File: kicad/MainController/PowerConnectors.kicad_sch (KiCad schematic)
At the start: 26 parts, among them J4 H-Bridge, J5 Lamp, J7 RGB, J8 Winch, J9 Motor, Q1 BC547, Q10 BUZ11, Q2 BUZ11, Q3 BC547, Q4 BUZ11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

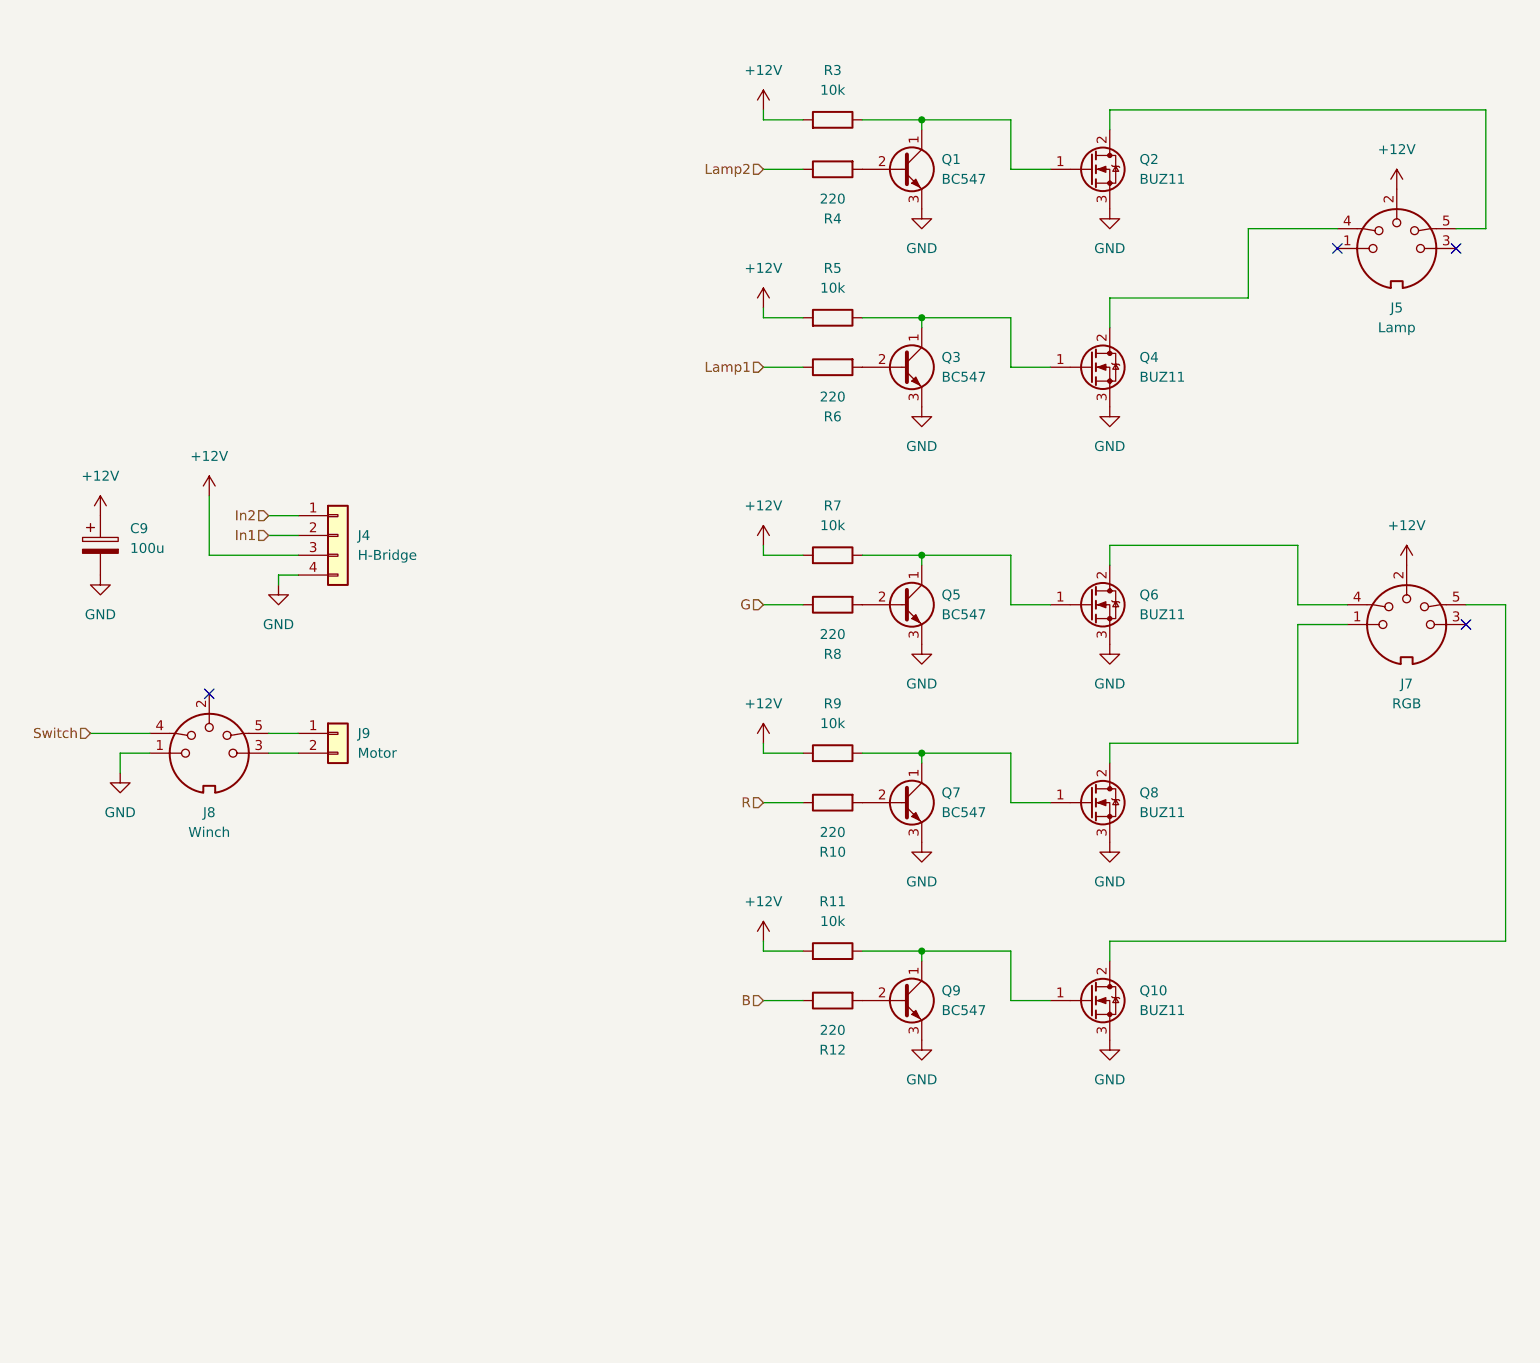
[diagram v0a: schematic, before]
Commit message: New main controller PCB layout using ESP32
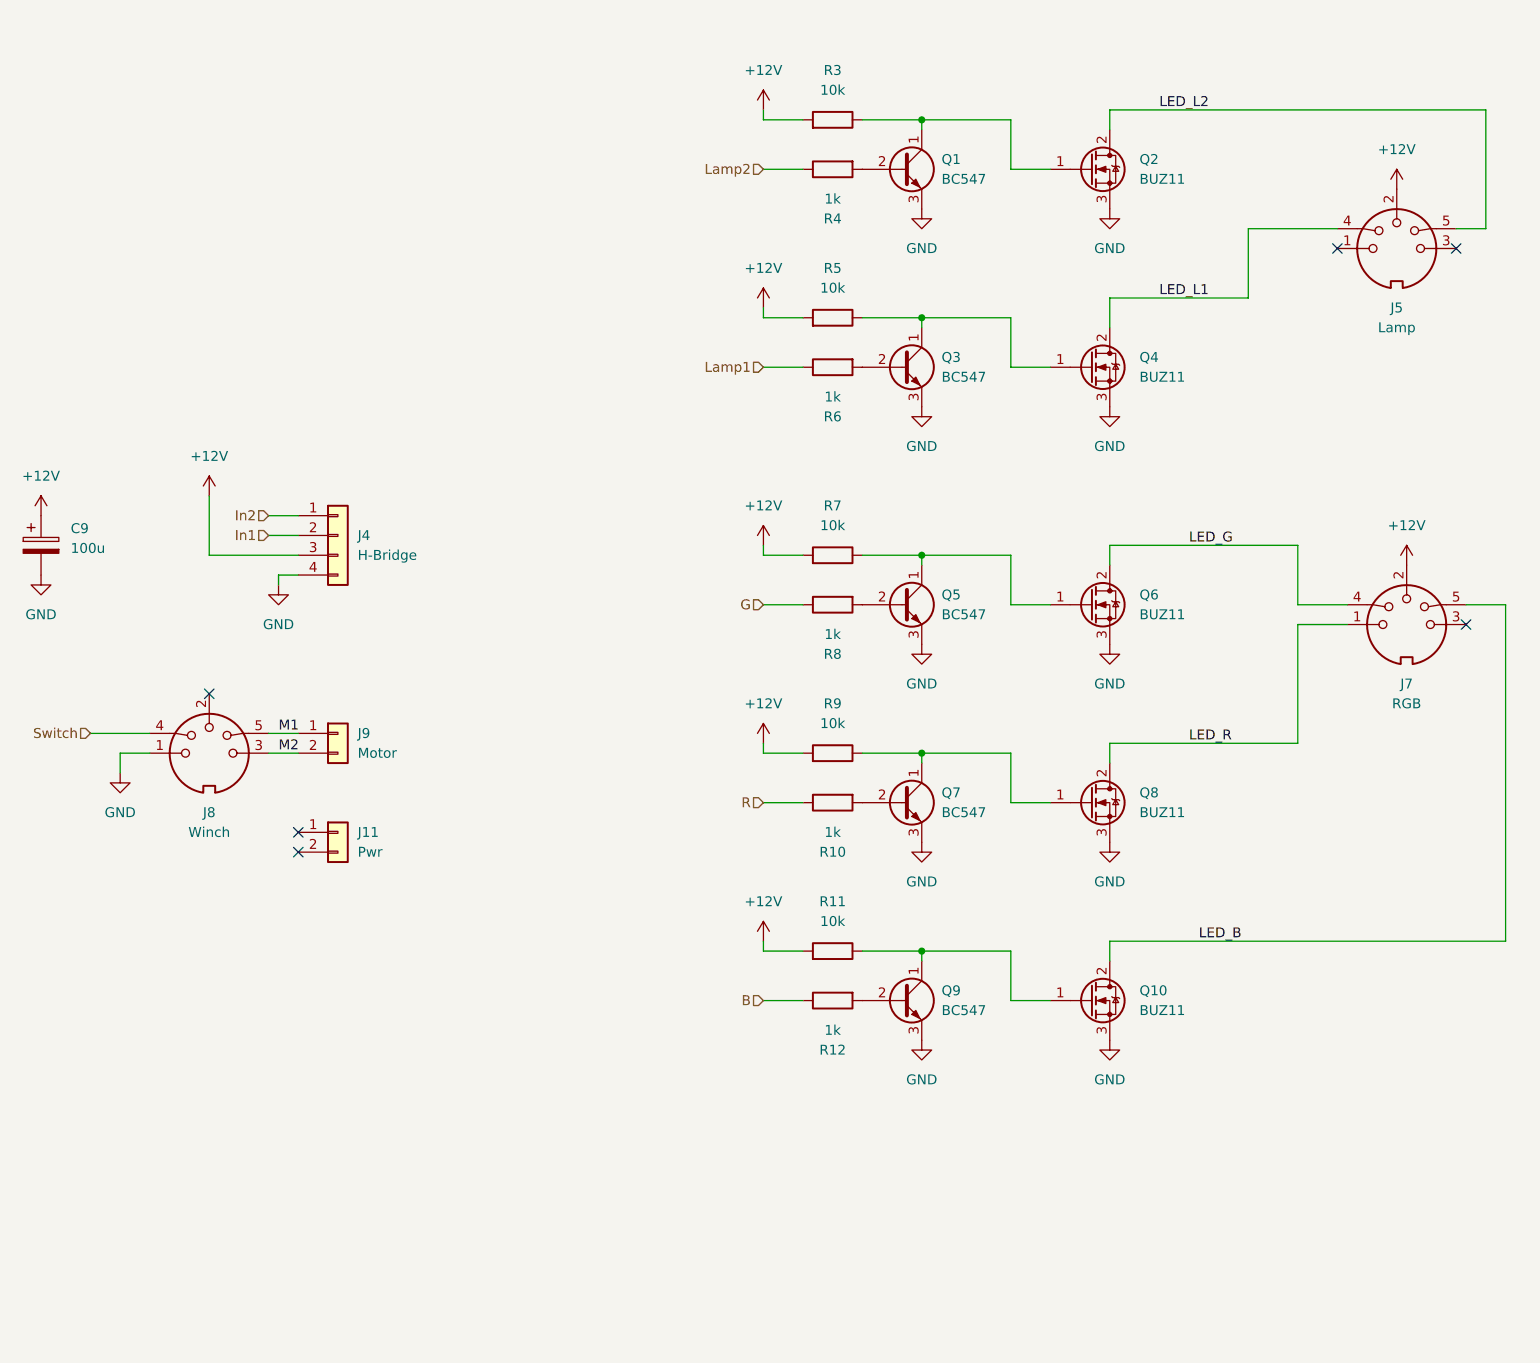
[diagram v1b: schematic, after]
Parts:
- added J11: Pwr, Connector_PinHeader_2.54mm:PinHeader_1x02_P2.54mm_Vertical, symbol Connector_Generic:Conn_01x02
- Q1, Q3, Q5, Q7, Q9: footprint Package_TO_SOT_THT:TO-92_Inline -> Custom_Footprints:TO-92_Milling
- R10, R12, R4, R6, R8: value 220 -> 1k; footprint Resistor_THT:R_Axial_DIN0204_L3.6mm_D1.6mm_P2.54mm_Vertical -> Resistor_THT:R_Axial_DIN0207_L6.3mm_D2.5mm_P10.16mm_Horizontal
- R11, R3, R5, R7, R9: footprint Resistor_THT:R_Axial_DIN0204_L3.6mm_D1.6mm_P2.54mm_Vertical -> Resistor_THT:R_Axial_DIN0207_L6.3mm_D2.5mm_P2.54mm_Vertical
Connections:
- net LED_L2: now reaches J5.5, Q2.2 (D)
- net LED_R: now reaches J7.1, Q8.2 (D)
- net LED_G: now reaches J7.4, Q6.2 (D)
- net LED_B: now reaches J7.5, Q10.2 (D)
- net LED_L1: now reaches J5.4, Q4.2 (D)
- net M1: now reaches J8.5, J9.1 (Pin_1)
- net M2: now reaches J8.3, J9.2 (Pin_2)
- no-connect marks 4 -> 6
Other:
- moved on the sheet: C9
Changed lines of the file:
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@@
 	)
 	(no_connect
+		(at 83.82 127)
+	)
+	(no_connect
 		(at 233.68 97.79)
 	)
@@
 	)
 	(no_connect
-		(at 232.41 49.53)
+		(at 83.82 124.46)
 	)
-	(wire
-		(pts
-			(xy 80.01 111.76) (xy 83.82 111.76)
-		)
-		(stroke
-			(width 0)
-			(type default)
-		)
+	(no_connect
+		(at 232.41 49.53)
 	)
 	(wire
@@
 	(wire
 		(pts
+			(xy 80.01 111.76) (xy 83.82 111.76)
+		)
+		(stroke
+			(width 0)
+			(type default)
+		)
+	)
+	(wire
+		(pts
 			(xy 156.21 139.7) (xy 163.83 139.7)
 		)
@@
 		)
 	)
+	(label "M2"
+		(at 81.28 114.3 0)
+		(effects
+			(font
+				(size 1.27 1.27)
+			)
+			(justify left bottom)
+		)
+	)
+	(label "M1"
+		(at 81.28 111.76 0)
+		(effects
+			(font
+				(size 1.27 1.27)
+			)
+			(justify left bottom)
+		)
+	)
+	(label "LED_B"
+		(at 199.39 138.43 0)
+		(effects
+			(font
+				(size 1.27 1.27)
+			)
+			(justify left bottom)
+		)
+	)
+	(label "LED_L1"
+		(at 194.31 55.88 0)
+		(effects
+			(font
+				(size 1.27 1.27)
+			)
+			(justify left bottom)
+		)
+	)
+	(label "LED_R"
+		(at 198.12 113.03 0)
+		(effects
+			(font
+				(size 1.27 1.27)
+			)
+			(justify left bottom)
+		)
+	)
+	(label "LED_G"
+		(at 198.12 87.63 0)
+		(effects
+			(font
+				(size 1.27 1.27)
+			)
+			(justify left bottom)
+		)
+	)
+	(label "LED_L2"
+		(at 194.31 31.75 0)
+		(effects
+			(font
+				(size 1.27 1.27)
+			)
+			(justify left bottom)
+		)
+	)
 	(hierarchical_label "B"
 		(shape input)
@@
 			)
 		)
-		(property "Footprint" "Resistor_THT:R_Axial_DIN0204_L3.6mm_D1.6mm_P2.54mm_Vertical"
+		(property "Footprint" "Resistor_THT:R_Axial_DIN0207_L6.3mm_D2.5mm_P2.54mm_Vertical"
 			(at 152.4 60.198 90)
 			(effects
@@
 			)
 		)
-		(property "Footprint" "Resistor_THT:R_Axial_DIN0204_L3.6mm_D1.6mm_P2.54mm_Vertical"
+		(property "Footprint" "Resistor_THT:R_Axial_DIN0207_L6.3mm_D2.5mm_P2.54mm_Vertical"
 			(at 152.4 116.078 90)
 			(effects
@@
 			)
 		)
-		(property "Footprint" "Package_TO_SOT_THT:TO-92_Inline"
+		(property "Footprint" "Custom_Footprints:TO-92_Milling"
 			(at 166.37 41.275 0)
 			(effects
@@
 			)
 		)
-		(property "Footprint" "Package_TO_SOT_THT:TO-92_Inline"
+		(property "Footprint" "Custom_Footprints:TO-92_Milling"
 			(at 166.37 66.675 0)
 			(effects
@@
 			)
 		)
-		(property "Footprint" "Resistor_THT:R_Axial_DIN0204_L3.6mm_D1.6mm_P2.54mm_Vertical"
+		(property "Footprint" "Resistor_THT:R_Axial_DIN0207_L6.3mm_D2.5mm_P2.54mm_Vertical"
 			(at 152.4 141.478 90)
 			(effects
@@
 			)
 		)
-		(property "Footprint" "Package_TO_SOT_THT:TO-92_Inline"
+		(property "Footprint" "Custom_Footprints:TO-92_Milling"
 			(at 166.37 97.155 0)
 			(effects
@@
 	)
 	(symbol
+		(lib_id "Connector_Generic:Conn_01x02")
+		(at 88.9 124.46 0)
+		(unit 1)
+		(exclude_from_sim no)
+		(in_bom yes)
+		(on_board yes)
+		(dnp no)
+		(fields_autoplaced yes)
+		(property "Reference" "J11"
+			(at 91.44 124.4599 0)
+			(effects
+				(font
+					(size 1.27 1.27)
+				)
+				(justify left)
+			)
+		)
+		(property "Value" "Pwr"
+			(at 91.44 126.9999 0)
+			(effects
+				(font
+					(size 1.27 1.27)
+				)
+				(justify left)
+			)
+		)
+		(property "Footprint" "Connector_PinHeader_2.54mm:PinHeader_1x02_P2.54mm_Vertical"
+			(at 88.9 124.46 0)
+			(effects
+				(font
+					(size 1.27 1.27)
+				)
+				(hide yes)
+			)
+		)
+		(property "Datasheet" "~"
+			(at 88.9 124.46 0)
+			(effects
+				(font
+					(size 1.27 1.27)
+				)
+				(hide yes)
+			)
+		)
+		(property "Description" "Generic connector, single row, 01x02, script generated (kicad-library-utils/schlib/autogen/connector/)"
+			(at 88.9 124.46 0)
+			(effects
+				(font
+					(size 1.27 1.27)
+				)
+				(hide yes)
+			)
+		)
+		(pin "1"
+		)
+		(pin "2"
+		)
+		(instances
+			(project "MainController"
+				(path "/bf87a95b-67d4-48e1-9f7e-6bce3e771984/211fff1a-1035-47e5-86a5-3692728681ac"
+					(reference "J11")
+					(unit 1)
+				)
+			)
+		)
+	)
+	(symbol
 		(lib_id "Transistor_FET:BUZ11")
 		(at 185.42 95.25 0)
@@
 			)
 		)
-		(property "Value" "220"
+		(property "Value" "1k"
 			(at 152.4 149.86 90)
 			(effects
@@
 			)
 		)
-		(property "Footprint" "Resistor_THT:R_Axial_DIN0204_L3.6mm_D1.6mm_P2.54mm_Vertical"
+		(property "Footprint" "Resistor_THT:R_Axial_DIN0207_L6.3mm_D2.5mm_P10.16mm_Horizontal"
 			(at 152.4 144.272 90)
 			(effects
@@
 			)
 		)
-		(property "Footprint" "Resistor_THT:R_Axial_DIN0204_L3.6mm_D1.6mm_P2.54mm_Vertical"
+		(property "Footprint" "Resistor_THT:R_Axial_DIN0207_L6.3mm_D2.5mm_P2.54mm_Vertical"
 			(at 152.4 34.798 90)
 			(effects
@@
 			)
 		)
-		(property "Footprint" "Package_TO_SOT_THT:TO-92_Inline"
+		(property "Footprint" "Custom_Footprints:TO-92_Milling"
 			(at 166.37 122.555 0)
 			(effects
@@
 			)
 		)
-		(property "Footprint" "Package_TO_SOT_THT:TO-92_Inline"
+		(property "Footprint" "Custom_Footprints:TO-92_Milling"
 			(at 166.37 147.955 0)
 			(effects
@@
 			)
 		)
-		(property "Value" "220"
+		(property "Value" "1k"
 			(at 152.4 43.18 90)
 			(effects
@@
 			)
 		)
-		(property "Footprint" "Resistor_THT:R_Axial_DIN0204_L3.6mm_D1.6mm_P2.54mm_Vertical"
+		(property "Footprint" "Resistor_THT:R_Axial_DIN0207_L6.3mm_D2.5mm_P10.16mm_Horizontal"
 			(at 152.4 37.592 90)
 			(effects
@@
 			)
 		)
-		(property "Footprint" "Resistor_THT:R_Axial_DIN0204_L3.6mm_D1.6mm_P2.54mm_Vertical"
+		(property "Footprint" "Resistor_THT:R_Axial_DIN0207_L6.3mm_D2.5mm_P2.54mm_Vertical"
 			(at 152.4 90.678 90)
 			(effects
@@
 			)
 		)
-		(property "Value" "220"
+		(property "Value" "1k"
 			(at 152.4 99.06 90)
 			(effects
@@
 			)
 		)
-		(property "Footprint" "Resistor_THT:R_Axial_DIN0204_L3.6mm_D1.6mm_P2.54mm_Vertical"
+		(property "Footprint" "Resistor_THT:R_Axial_DIN0207_L6.3mm_D2.5mm_P10.16mm_Horizontal"
 			(at 152.4 93.472 90)
 			(effects
@@
 	(symbol
 		(lib_id "power:GND")
-		(at 58.42 91.44 0)
+		(at 50.8 91.44 0)
 		(unit 1)
 		(exclude_from_sim no)
@@
 		(fields_autoplaced yes)
 		(property "Reference" "#PWR024"
-			(at 58.42 97.79 0)
+			(at 50.8 97.79 0)
 			(effects
 				(font
@@
 		)
 		(property "Value" "GND"
-			(at 58.42 96.52 0)
+			(at 50.8 96.52 0)
 			(effects
 				(font
@@
 		)
 		(property "Footprint" ""
-			(at 58.42 91.44 0)
+			(at 50.8 91.44 0)
 			(effects
 				(font
@@
 		)
 		(property "Datasheet" ""
-			(at 58.42 91.44 0)
+			(at 50.8 91.44 0)
 			(effects
 				(font
@@
 		)
 		(property "Description" "Power symbol creates a global label with name \"GND\" , ground"
-			(at 58.42 91.44 0)
+			(at 50.8 91.44 0)
 			(effects
 				(font
@@
 			)
 		)
-		(property "Value" "220"
+		(property "Value" "1k"
 			(at 152.4 68.58 90)
 			(effects
@@
 			)
 		)
-		(property "Footprint" "Resistor_THT:R_Axial_DIN0204_L3.6mm_D1.6mm_P2.54mm_Vertical"
+		(property "Footprint" "Resistor_THT:R_Axial_DIN0207_L6.3mm_D2.5mm_P10.16mm_Horizontal"
 			(at 152.4 62.992 90)
 			(effects
@@
 	(symbol
 		(lib_id "Device:C_Polarized")
-		(at 58.42 87.63 0)
+		(at 50.8 87.63 0)
 		(unit 1)
 		(exclude_from_sim no)
@@
 		(fields_autoplaced yes)
 		(property "Reference" "C9"
-			(at 62.23 85.4709 0)
+			(at 54.61 85.4709 0)
 			(effects
 				(font
@@
 		)
 		(property "Value" "100u"
-			(at 62.23 88.0109 0)
+			(at 54.61 88.0109 0)
 			(effects
 				(font
@@
 		)
 		(property "Footprint" "Capacitor_THT:CP_Radial_D7.5mm_P2.50mm"
-			(at 59.3852 91.44 0)
+			(at 51.7652 91.44 0)
 			(effects
 				(font
@@
 		)
 		(property "Datasheet" "~"
-			(at 58.42 87.63 0)
+			(at 50.8 87.63 0)
 			(effects
 				(font
@@
 		)
 		(property "Description" "Polarized capacitor"
-			(at 58.42 87.63 0)
+			(at 50.8 87.63 0)
 			(effects
 				(font
@@
 	(symbol
 		(lib_id "power:+12V")
-		(at 58.42 83.82 0)
+		(at 50.8 83.82 0)
 		(unit 1)
 		(exclude_from_sim no)
@@
 		(fields_autoplaced yes)
 		(property "Reference" "#PWR023"
-			(at 58.42 87.63 0)
+			(at 50.8 87.63 0)
 			(effects
 				(font
@@
 		)
 		(property "Value" "+12V"
-			(at 58.42 78.74 0)
+			(at 50.8 78.74 0)
 			(effects
 				(font
@@
 		)
 		(property "Footprint" ""
-			(at 58.42 83.82 0)
+			(at 50.8 83.82 0)
 			(effects
 				(font
@@
 		)
 		(property "Datasheet" ""
-			(at 58.42 83.82 0)
+			(at 50.8 83.82 0)
 			(effects
 				(font
@@
 		)
 		(property "Description" "Power symbol creates a global label with name \"+12V\""
-			(at 58.42 83.82 0)
+			(at 50.8 83.82 0)
 			(effects
 				(font
@@
 			)
 		)
-		(property "Value" "220"
+		(property "Value" "1k"
 			(at 152.4 124.46 90)
 			(effects
@@
 			)
 		)
-		(property "Footprint" "Resistor_THT:R_Axial_DIN0204_L3.6mm_D1.6mm_P2.54mm_Vertical"
+		(property "Footprint" "Resistor_THT:R_Axial_DIN0207_L6.3mm_D2.5mm_P10.16mm_Horizontal"
 			(at 152.4 118.872 90)
 			(effects

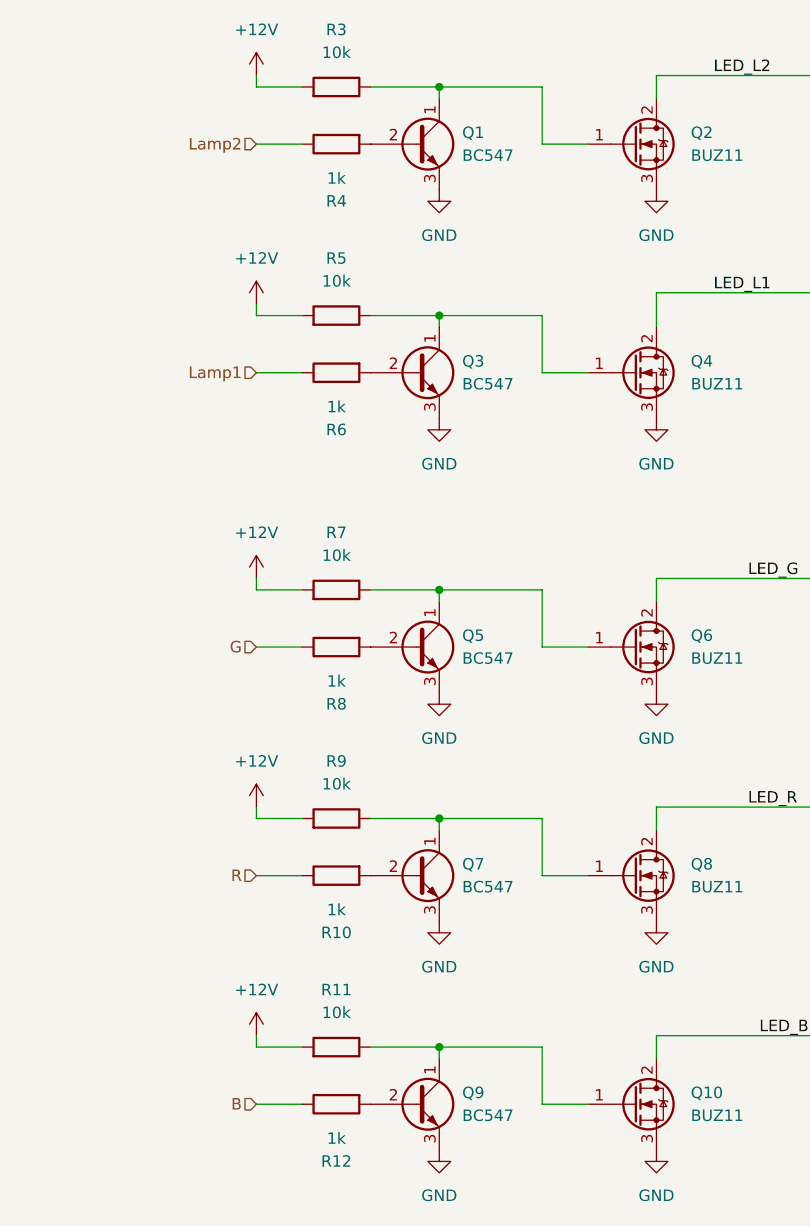
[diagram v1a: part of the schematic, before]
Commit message: Updated main controller implementation for ESP32
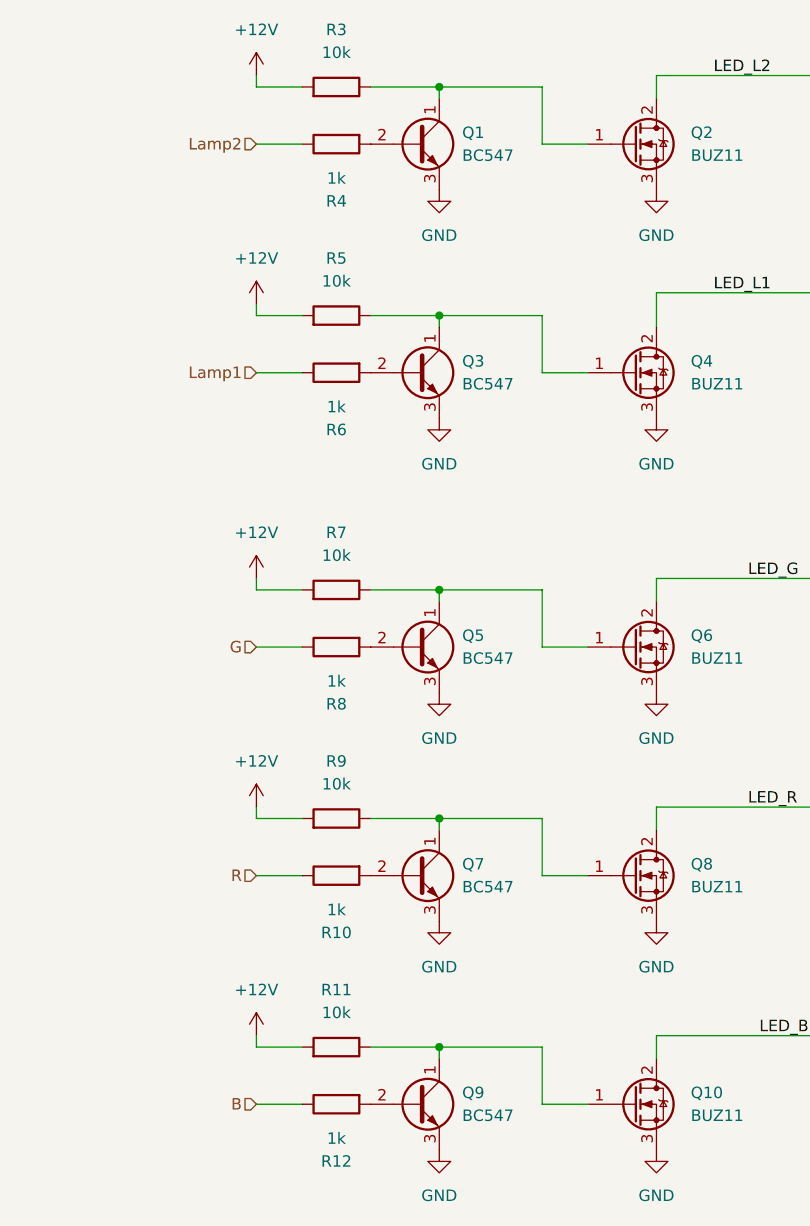
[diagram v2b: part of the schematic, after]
